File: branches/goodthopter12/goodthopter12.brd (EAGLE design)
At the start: 73 x 35.6 mm, 28 parts, among them IC1 F22X4---DA38, IC2 FT232RL-BASICSSOP, Q2 20MHz

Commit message: GoodThopter12 mods.  Geting closer to manufacturing.
git-svn-id: https://svn.code.sf.net/p/goodfet/code@1565 12e2690d-a6be-4b82-a7b7-67c4a43b65c8
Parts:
- removed CAN_IO: (no value), con-lstb:MA06-1
- moved R3 37.9 mm to (21.9, 5.40)
- moved R2 37.8 mm to (21.9, 3.17)
- moved TX_LED 37.3 mm to (25.7, 5.40)
- moved RX_LED 37.2 mm to (25.7, 3.17)
- moved R6 14.0 mm to (54.6, 16.5), turned to 180 degrees
- moved C6 12.8 mm to (42.5, 30.8)
- moved R5 10.6 mm to (54.6, 23.8)
- moved R7 9.38 mm to (54.6, 21.3)
- moved C5 5.91 mm to (46.7, 14.6), turned to 0 degrees
- moved R8 4.41 mm to (54.6, 14.3), turned to 0 degrees
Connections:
- removed net CAN_V+_OPT: CAN(12V).9
- removed net GND_OPT: CAN(12V).6
- removed net RSRVD0: CAN(12V).1
- removed net RSRVD1: CAN(12V).4
- removed net RSRVD2: CAN(12V).8
- new net N$11: CAN(12V).5, R5.2
- new net N$12: CAN(12V).7, R6.1
- new net N$3: CAN(12V).2, R8.2
- new net N$4: CAN(12V).3, R7.2
- net !TX0RTS: no longer CAN_IO.4
- net !TX1RTS: no longer CAN_IO.5
- net !TX2RTS: no longer CAN_IO.6
- net CANH: now also R6.2; no longer CAN(12V).3, CAN(12V).7, R5.1, R5.2, R7.2
- net CANL: now also R5.1; no longer CAN(12V).2, CAN(12V).5, R6.1, R6.2, R8.2
- net CLKOUT: no longer CAN_IO.3
- net RXCAN: no longer CAN_IO.2
- net TXCAN: no longer CAN_IO.1
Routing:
- net CANH: track 68.6 -> 13.5 mm, vias 4 -> 0
- net CANL: track 42.9 -> 17.9 mm, vias 6 -> 0
- net TXCAN: track 52.9 -> 31.4 mm
- net RXCAN: track 49.7 -> 35.3 mm, vias 2 -> 0
- net VCC: track 109.5 -> 121.5 mm, vias 3 -> 4
- net N$12: track 0.00 -> 9.55 mm
- net VCC5V: track 73.0 -> 64.3 mm
- net !TX2RTS: track 8.43 -> 0.00 mm, vias 1 -> 0
- net !TX1RTS: track 8.43 -> 0.00 mm
- net N$4: track 0.00 -> 7.94 mm
- net N$3: track 0.00 -> 7.05 mm
- net N$11: track 0.00 -> 6.69 mm
- net !TX0RTS: track 5.24 -> 0.00 mm
- net CLKOUT: track 4.42 -> 0.00 mm
- net GND: track 35.7 -> 39.4 mm
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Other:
- board text added: "Pop for ICS"
- board text added: "Pop for Sparkfun"

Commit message: Renamed some LEDs.  Closer to ordering GoodThopter12 boards.
git-svn-id: https://svn.code.sf.net/p/goodfet/code@1566 12e2690d-a6be-4b82-a7b7-67c4a43b65c8
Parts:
- moved C3 7.43 mm to (43.2, 7.62)
- moved Q2 6.25 mm to (47.3, 3.17)
- moved C2 3.82 mm to (51.8, 7.62), turned to 180 degrees
- renumbered RXLED to USBRX, RX_LED to CANRX, TXLED to USBTX, TX_LED to CANTX
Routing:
- net OSC2: track 30.2 -> 21.5 mm
- net OSC1: track 16.8 -> 11.0 mm, vias 2 -> 0
- net GND: track 39.4 -> 34.2 mm

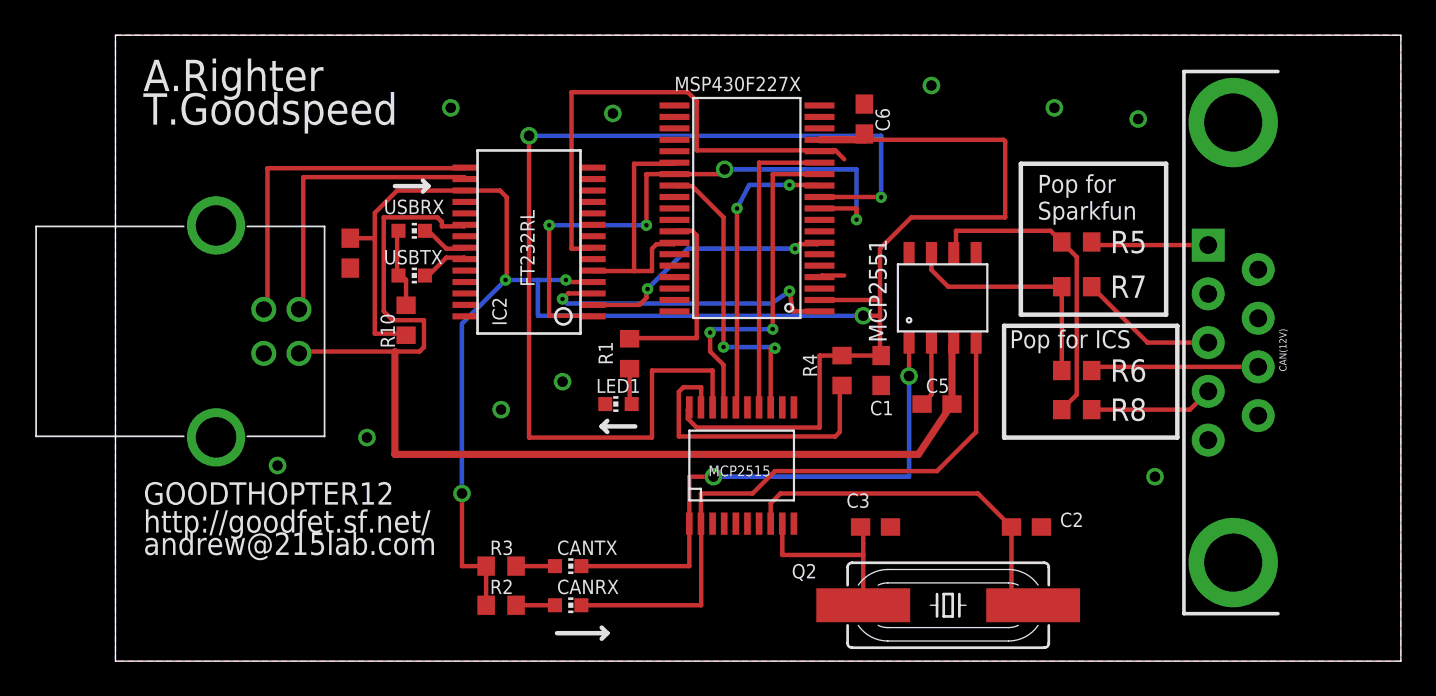
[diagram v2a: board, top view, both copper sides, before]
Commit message: Now the Sparkfun cable is default in the GoodThopter12. You can cut two traces and add two SMD resistors to use the older cable.
git-svn-id: https://svn.code.sf.net/p/goodfet/code@1567 12e2690d-a6be-4b82-a7b7-67c4a43b65c8
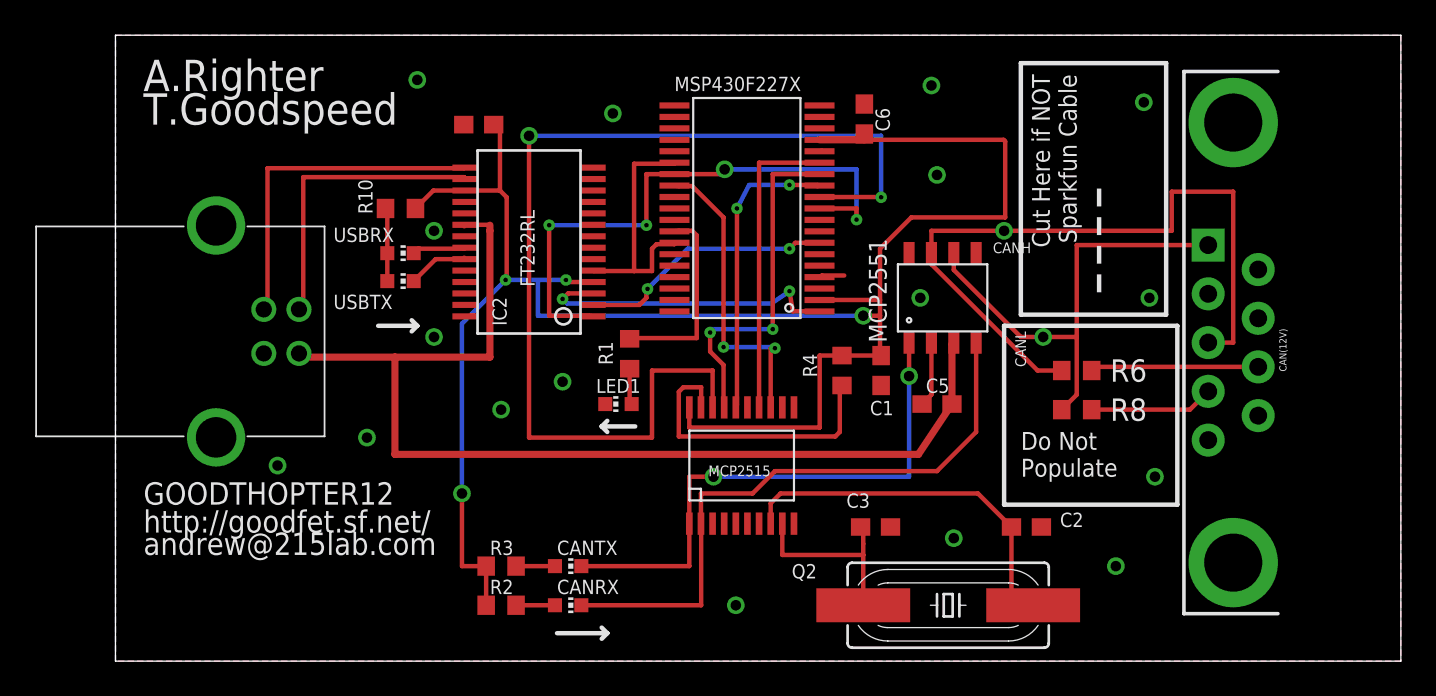
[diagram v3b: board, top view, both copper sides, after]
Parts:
- removed R5, R7: 0, rcl:R0603
- moved C4 10.3 mm to (20.6, 30.5), turned to 0 degrees
- moved R10 6.36 mm to (16.2, 25.7), turned to 0 degrees
- moved USBRX 1.42 mm to (16.2, 23.2)
- moved USBTX 0.71 mm to (16.2, 21.6)
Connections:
- removed net N$11: CAN(12V).5, R5.2
- removed net N$4: CAN(12V).3, R7.2
- net CANH: now also CAN(12V).3; no longer R7.1
- net CANL: now also CAN(12V).5; no longer R5.1
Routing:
- net GND: track 34.2 -> 5.52 mm, vias 10 -> 17
- net CANH: track 13.5 -> 41.2 mm, vias 0 -> 1
- net CANL: track 17.9 -> 26.8 mm, vias 0 -> 1
- net VCC: track 121.5 -> 113.1 mm
- net N$4: track 7.94 -> 0.00 mm
- net N$11: track 6.69 -> 0.00 mm
- net VCC5V: track 64.3 -> 62.8 mm
- net N$7: track 2.75 -> 3.50 mm
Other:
- board text added: "CANH"
- board text added: "CANL"
- board text added: "Cut Here if NOT Sparkfun Cable"
- board text added: "Do Not Populate"
- board text removed: "Pop for ICS"
- board text removed: "Pop for Sparkfun"

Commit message: Final fixes for GT12.  Gerbers coming in the next commit.
git-svn-id: https://svn.code.sf.net/p/goodfet/code@1570 12e2690d-a6be-4b82-a7b7-67c4a43b65c8
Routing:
- net MOSI: track 16.9 -> 17.5 mm
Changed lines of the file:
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@@
 <setting verticaltext="up"/>
 </settings>
-<grid distance="0.0125" unitdist="inch" unit="inch" style="lines" multiple="1" display="no" altdistance="0.0001" altunitdist="inch" altunit="inch"/>
+<grid distance="0.0125" unitdist="inch" unit="inch" style="lines" multiple="1" display="no" altdistance="0.005" altunitdist="inch" altunit="inch"/>
 <layers>
 <layer number="1" name="Top" color="4" fill="1" visible="yes" active="yes"/>
@@
 <contactref element="U$1" pad="16"/>
 <wire x1="35.306" y1="25.7175" x2="35.306" y2="14.5415" width="0.254" layer="1"/>
-<wire x1="36.0045" y1="27.051" x2="35.306" y2="25.7175" width="0.254" layer="16"/>
-<wire x1="38.2905" y1="27.051" x2="36.0045" y2="27.051" width="0.254" layer="16"/>
 <wire x1="35.306" y1="14.5415" x2="35.2425" y2="14.4145" width="0.254" layer="1"/>
 <wire x1="39.878" y1="26.9875" x2="39.9975" y2="27.0175" width="0.254" layer="1"/>
 <via x="35.306" y="25.7175" extent="1-16" drill="0.254"/>
-<via x="38.2905" y="27.051" extent="1-16" drill="0.254"/>
 <wire x1="39.878" y1="26.9875" x2="39.878" y2="27.051" width="0.254" layer="1"/>
-<wire x1="39.878" y1="27.051" x2="38.2905" y2="27.051" width="0.254" layer="1"/>
+<wire x1="35.306" y1="25.7175" x2="38.227" y2="25.7175" width="0.254" layer="16"/>
+<via x="38.227" y="25.7175" extent="1-16" drill="0.5"/>
+<wire x1="38.227" y1="25.7175" x2="38.227" y2="27.0175" width="0.254" layer="1"/>
+<wire x1="38.227" y1="27.0175" x2="39.9975" y2="27.0175" width="0.254" layer="1"/>
 </signal>
 <signal name="MISO">
@@
 <wire x1="63.5" y1="18.0975" x2="63.5" y2="26.67" width="0.254" layer="1"/>
 <wire x1="63.5" y1="26.67" x2="60.0075" y2="26.67" width="0.254" layer="1"/>
-<wire x1="60.0075" y1="26.67" x2="60.0075" y2="24.4475" width="0.254" layer="1"/>
-<wire x1="60.0075" y1="24.4475" x2="50.4825" y2="24.4475" width="0.254" layer="1"/>
-<wire x1="50.4825" y1="24.4475" x2="46.355" y2="24.4475" width="0.254" layer="1"/>
-<wire x1="46.355" y1="24.4475" x2="46.355" y2="23.1775" width="0.254" layer="1"/>
-<via x="50.4825" y="24.4475" extent="1-16" drill="0.6" shape="square"/>
+<wire x1="60.0075" y1="26.67" x2="60.0075" y2="24.13" width="0.254" layer="1"/>
+<wire x1="60.0075" y1="24.13" x2="50.4825" y2="24.13" width="0.254" layer="1"/>
+<via x="50.4825" y="24.13" extent="1-16" drill="0.6" shape="square"/>
+<wire x1="46.355" y1="23.1775" x2="46.355" y2="24.4475" width="0.254" layer="1"/>
+<wire x1="46.355" y1="24.4475" x2="50.165" y2="24.4475" width="0.254" layer="1"/>
+<wire x1="50.165" y1="24.4475" x2="50.4825" y2="24.13" width="0.254" layer="1"/>
 </signal>
 <signal name="N$1">
